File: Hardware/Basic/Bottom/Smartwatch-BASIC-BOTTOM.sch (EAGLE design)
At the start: 35 parts, among them U1 AD5242-SO16, U3 PCF8523

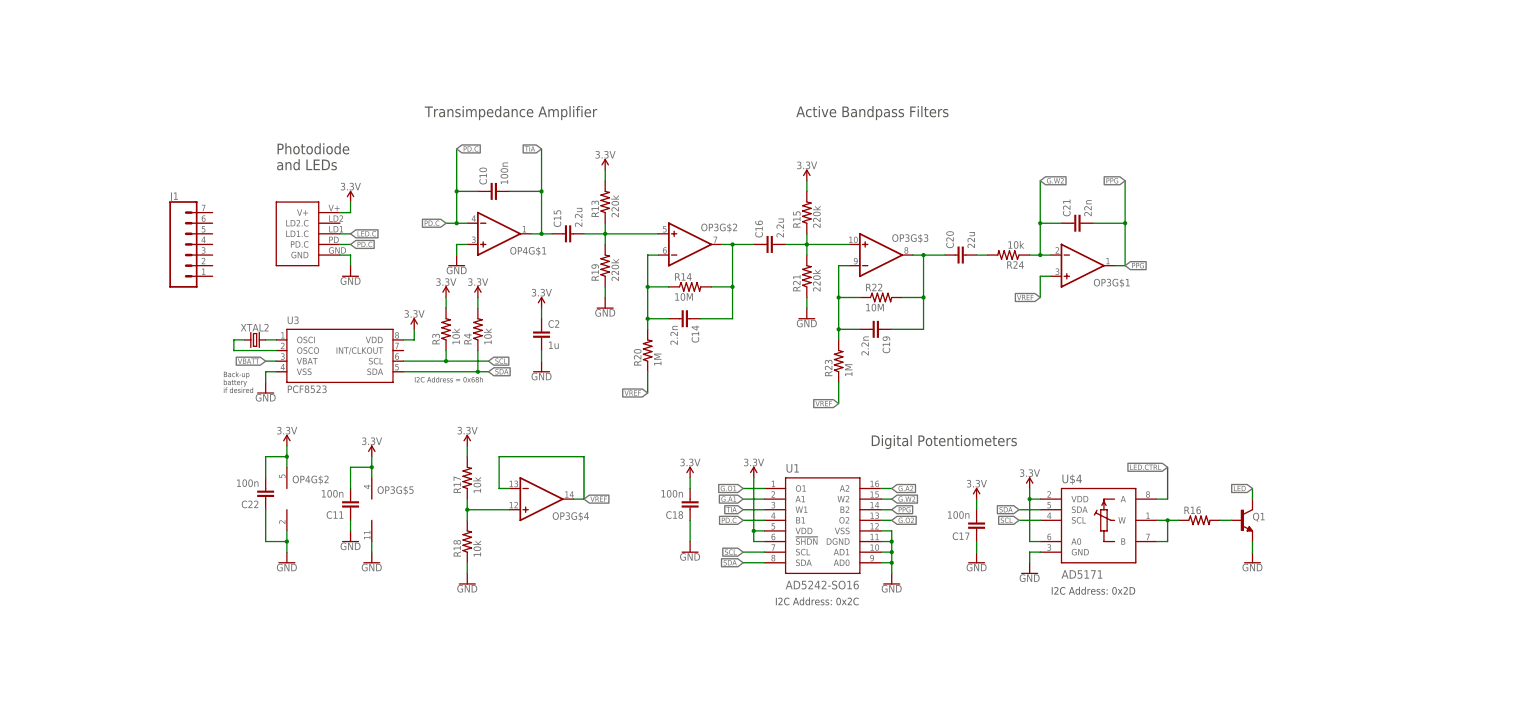
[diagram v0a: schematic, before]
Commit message: Bottom board routed
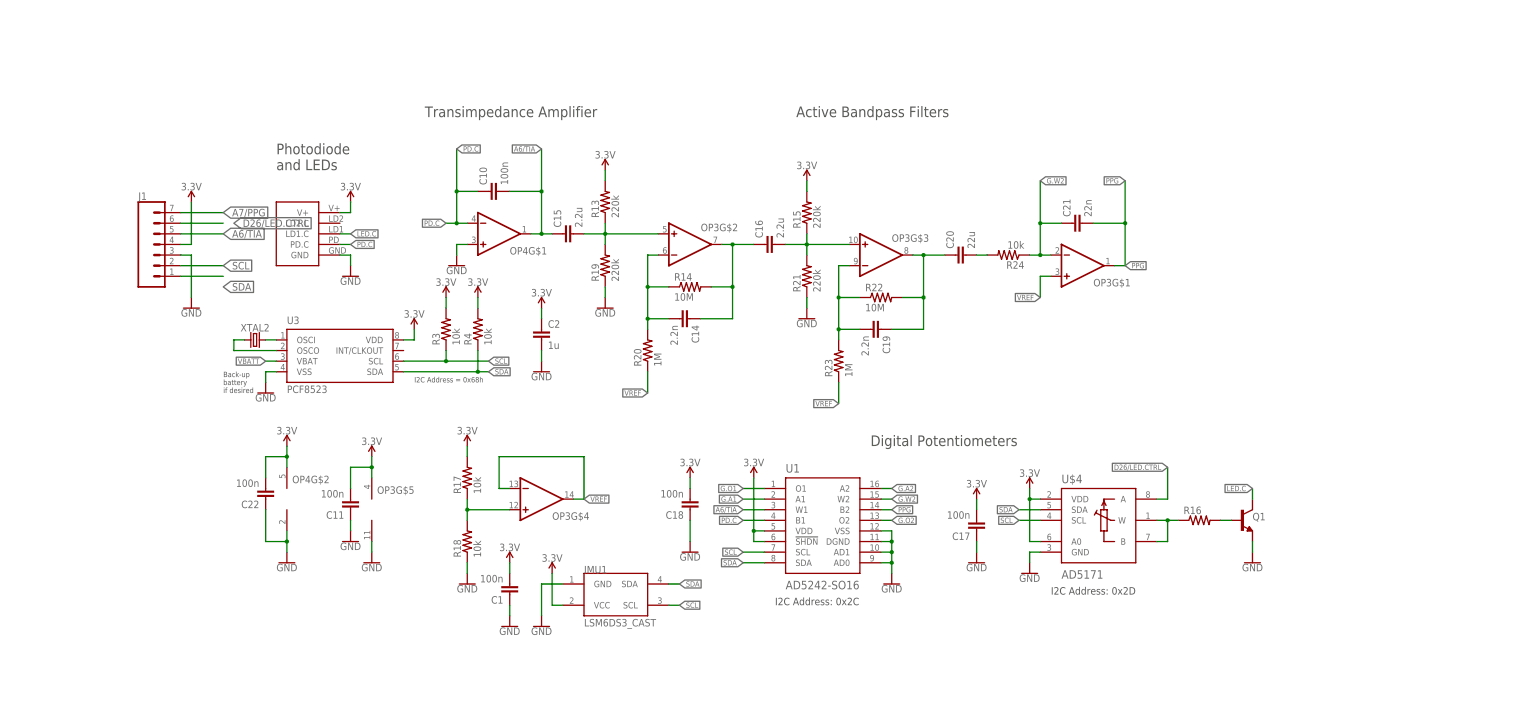
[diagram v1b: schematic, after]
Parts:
- added C1: 100n, LinnesLab-Passives:CAPACITOR0603
- added IMU1: LSM6DS3_CAST, LinnesLab-Sensors:LSM6DS3_CAST
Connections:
- removed net LED: Q1.C
- removed net LED.CTRL: U$4.A
- removed net TIA: C10.2, C15.1, OP4G$1.OUT, U1.W1
- new net A6/TIA: C10.2, C15.1, J1.5, OP4G$1.OUT, U1.W1
- new net A7/PPG: J1.7
- new net D26/LED.CTRL: J1.6, U$4.A
- net 3.3V: now also C1.2, IMU1.VCC, J1.4
- net GND: now also C1.1, IMU1.GND, J1.3
- net LED.C: now also Q1.C
- net SCL: now also IMU1.SCL, J1.2
- net SDA: now also IMU1.SDA, J1.1
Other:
- moved on the sheet: J1

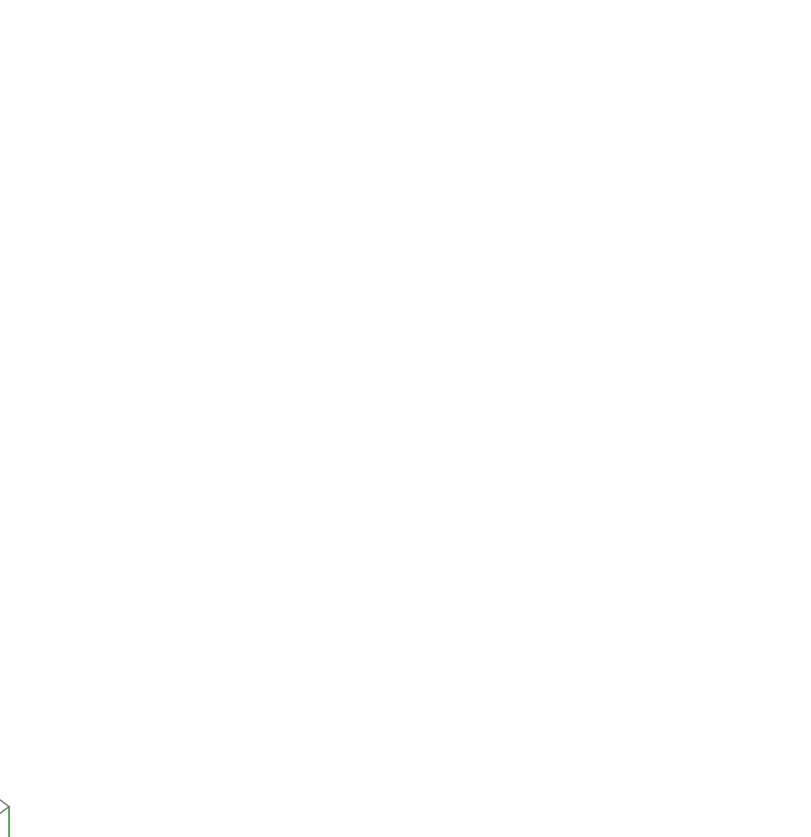
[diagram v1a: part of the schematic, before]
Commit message: Rearranging Top Board
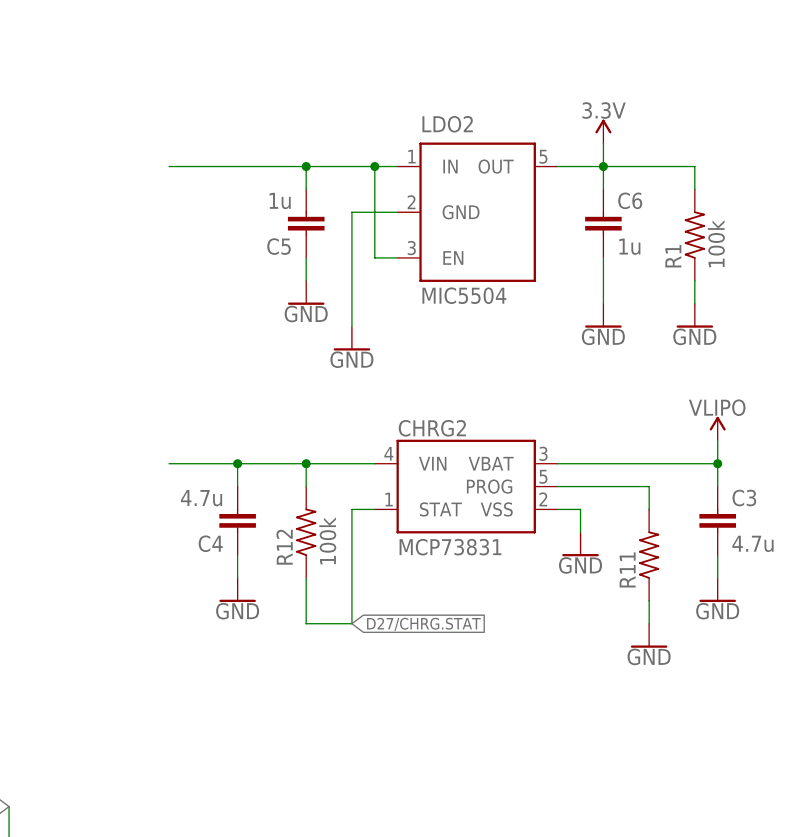
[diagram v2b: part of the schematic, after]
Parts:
- added C3, C4: 4.7u, LinnesLab-Passives:CAPACITOR0603
- added C5, C6: 1u, LinnesLab-Passives:CAPACITOR0603
- added CHRG2: MCP73831, LinnesLab-Power:MCP73831
- added LDO2: MIC5504, LinnesLab-Power:MIC5504
- added R1, R12: 100k, LinnesLab-Passives:RESISTOR0603
- added R11: (no value), LinnesLab-Passives:RESISTOR0603
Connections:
- new net D27/CHRG.STAT: CHRG2.STAT, R12.1
- new net N$1: CHRG2.PROG, R11.2
- new net VIN1: C4.2, C5.2, CHRG2.VIN, LDO2.EN, LDO2.IN, R12.2
- new net VLIPO: C3.1, CHRG2.VBAT
- net 3.3V: now also C6.1, LDO2.OUT, R1.2
- net GND: now also C3.2, C4.1, C5.1, C6.2, CHRG2.VSS, LDO2.GND, R1.1, R11.1

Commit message: Rearranged Top Board
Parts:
- removed C3, C4: 4.7u, LinnesLab-Passives:CAPACITOR0603
- removed C5, C6: 1u, LinnesLab-Passives:CAPACITOR0603
- removed CHRG2: MCP73831, LinnesLab-Power:MCP73831
- removed LDO2: MIC5504, LinnesLab-Power:MIC5504
- removed R1, R12: 100k, LinnesLab-Passives:RESISTOR0603
- removed R11: (no value), LinnesLab-Passives:RESISTOR0603
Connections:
- removed net D27/CHRG.STAT: CHRG2.STAT, R12.1
- removed net N$1: CHRG2.PROG, R11.2
- removed net VIN1: C4.2, C5.2, CHRG2.VIN, LDO2.EN, LDO2.IN, R12.2
- removed net VLIPO: C3.1, CHRG2.VBAT
- net 3.3V: no longer C6.1, LDO2.OUT, R1.2
- net GND: no longer C3.2, C4.1, C5.1, C6.2, CHRG2.VSS, LDO2.GND, R1.1, R11.1

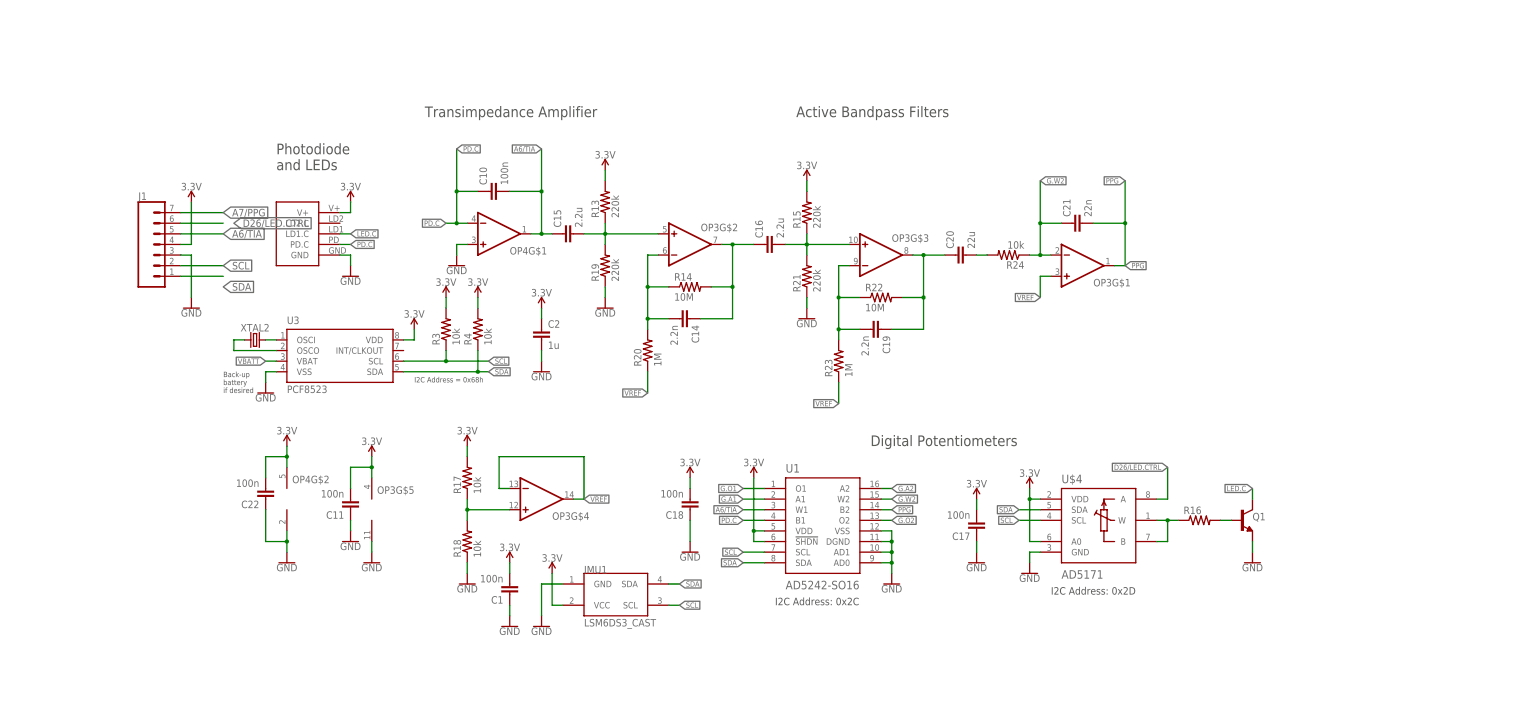
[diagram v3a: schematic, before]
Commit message: Organized Schematics and Silkscreens for both boards
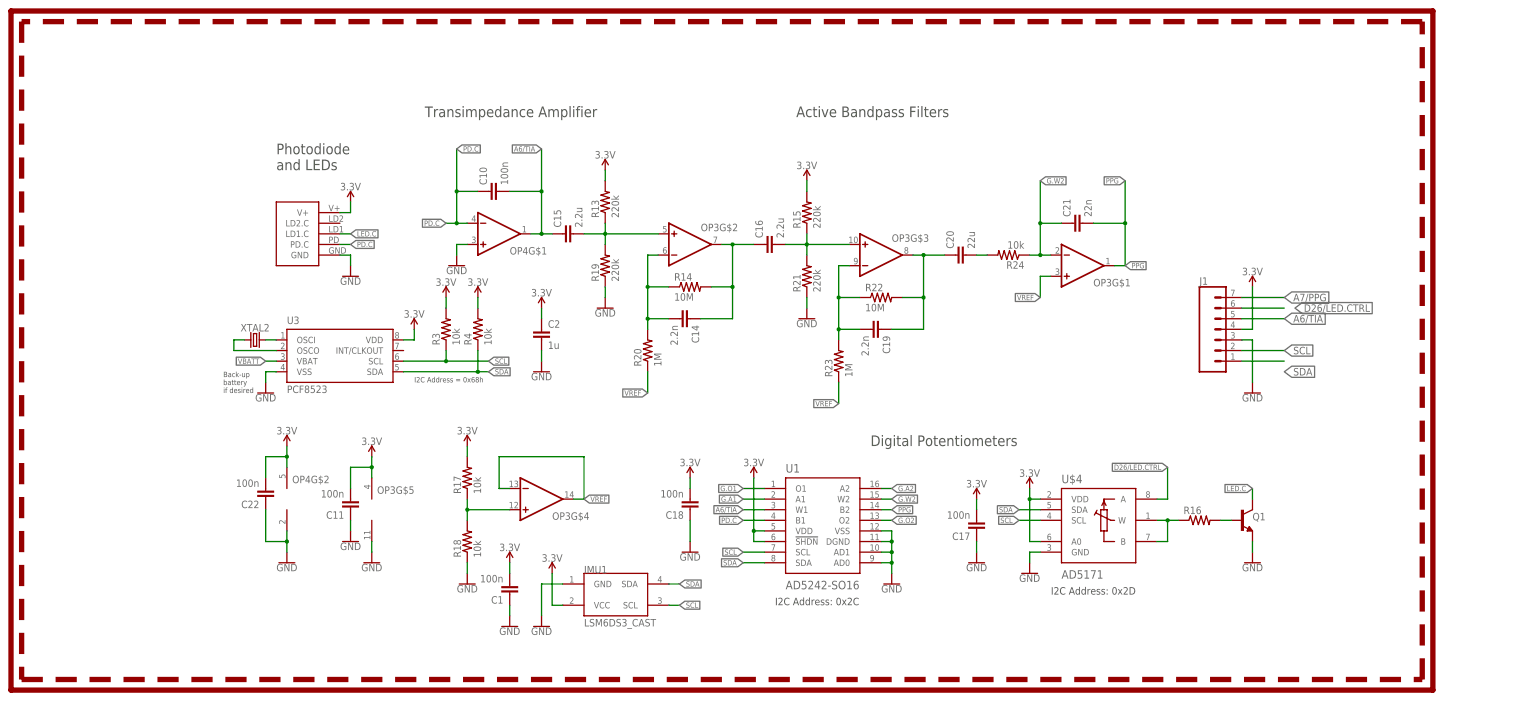
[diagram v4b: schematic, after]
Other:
- moved on the sheet: J1
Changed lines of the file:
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@@
 battery
 if desired</text>
+<wire x1="-114.3" y1="114.3" x2="-114.3" y2="-43.18" width="1.27" layer="94" style="longdash"/>
+<wire x1="-114.3" y1="-43.18" x2="220.98" y2="-43.18" width="1.27" layer="94" style="longdash"/>
+<wire x1="220.98" y1="-43.18" x2="220.98" y2="114.3" width="1.27" layer="94" style="longdash"/>
+<wire x1="220.98" y1="114.3" x2="-114.3" y2="114.3" width="1.27" layer="94" style="longdash"/>
+<wire x1="-116.84" y1="116.84" x2="223.52" y2="116.84" width="1.27" layer="94"/>
+<wire x1="223.52" y1="116.84" x2="223.52" y2="-45.72" width="1.27" layer="94"/>
+<wire x1="223.52" y1="-45.72" x2="-116.84" y2="-45.72" width="1.27" layer="94"/>
+<wire x1="-116.84" y1="-45.72" x2="-116.84" y2="116.84" width="1.27" layer="94"/>
 </plain>
 <instances>
@@
 <attribute name="MFN_MANUFACTURER" x="-38.1" y="35.56" size="1.27" layer="96" display="off"/>
 </instance>
-<instance part="J1" gate="G$1" x="-81.28" y="58.42" smashed="yes">
-<attribute name="VALUE" x="-86.36" y="48.514" size="1.778" layer="96" font="vector"/>
-<attribute name="NAME" x="-86.36" y="71.628" size="1.778" layer="95" font="vector"/>
+<instance part="J1" gate="G$1" x="172.72" y="38.1" smashed="yes">
+<attribute name="VALUE" x="167.64" y="28.194" size="1.778" layer="96" font="vector"/>
+<attribute name="NAME" x="167.64" y="51.308" size="1.778" layer="95" font="vector"/>
 </instance>
 <instance part="IMU1" gate="G$1" x="27.94" y="-22.86" smashed="yes">
@@
 <attribute name="VALUE" x="2.54" y="-12.446" size="1.778" layer="96" align="bottom-center"/>
 </instance>
-<instance part="GND6" gate="G$1" x="-73.66" y="45.72" smashed="yes">
-<attribute name="VALUE" x="-73.66" y="45.466" size="1.778" layer="96" align="top-center"/>
-</instance>
-<instance part="SUPPLY1" gate="G$1" x="-73.66" y="71.12" smashed="yes">
-<attribute name="VALUE" x="-73.66" y="73.914" size="1.778" layer="96" align="bottom-center"/>
+<instance part="GND6" gate="G$1" x="180.34" y="25.4" smashed="yes">
+<attribute name="VALUE" x="180.34" y="25.146" size="1.778" layer="96" align="top-center"/>
+</instance>
+<instance part="SUPPLY1" gate="G$1" x="180.34" y="50.8" smashed="yes">
+<attribute name="VALUE" x="180.34" y="53.594" size="1.778" layer="96" align="bottom-center"/>
 </instance>
 </instances>
@@
 <pinref part="J1" gate="G$1" pin="3"/>
 <pinref part="GND6" gate="G$1" pin="GND"/>
-<wire x1="-76.2" y1="58.42" x2="-73.66" y2="58.42" width="0.1524" layer="91"/>
-<wire x1="-73.66" y1="58.42" x2="-73.66" y2="48.26" width="0.1524" layer="91"/>
+<wire x1="177.8" y1="38.1" x2="180.34" y2="38.1" width="0.1524" layer="91"/>
+<wire x1="180.34" y1="38.1" x2="180.34" y2="27.94" width="0.1524" layer="91"/>
 </segment>
 </net>
@@
 <pinref part="J1" gate="G$1" pin="4"/>
 <pinref part="SUPPLY1" gate="G$1" pin="3.3V"/>
-<wire x1="-76.2" y1="60.96" x2="-73.66" y2="60.96" width="0.1524" layer="91"/>
-<wire x1="-73.66" y1="60.96" x2="-73.66" y2="71.12" width="0.1524" layer="91"/>
+<wire x1="177.8" y1="40.64" x2="180.34" y2="40.64" width="0.1524" layer="91"/>
+<wire x1="180.34" y1="40.64" x2="180.34" y2="50.8" width="0.1524" layer="91"/>
 </segment>
 </net>
@@
 <segment>
 <pinref part="J1" gate="G$1" pin="1"/>
-<wire x1="-76.2" y1="53.34" x2="-66.04" y2="53.34" width="0.1524" layer="91"/>
-<label x="-66.04" y="50.8" size="1.778" layer="95" xref="yes"/>
+<wire x1="177.8" y1="33.02" x2="187.96" y2="33.02" width="0.1524" layer="91"/>
+<label x="187.96" y="30.48" size="1.778" layer="95" xref="yes"/>
 </segment>
 </net>
@@
 <segment>
 <pinref part="J1" gate="G$1" pin="2"/>
-<wire x1="-76.2" y1="55.88" x2="-66.04" y2="55.88" width="0.1524" layer="91"/>
-<label x="-66.04" y="55.88" size="1.778" layer="95" xref="yes"/>
+<wire x1="177.8" y1="35.56" x2="187.96" y2="35.56" width="0.1524" layer="91"/>
+<label x="187.96" y="35.56" size="1.778" layer="95" xref="yes"/>
 </segment>
 </net>
@@
 <segment>
 <pinref part="J1" gate="G$1" pin="5"/>
-<wire x1="-76.2" y1="63.5" x2="-66.04" y2="63.5" width="0.1524" layer="91"/>
-<label x="-66.04" y="63.5" size="1.778" layer="95" xref="yes"/>
+<wire x1="177.8" y1="43.18" x2="187.96" y2="43.18" width="0.1524" layer="91"/>
+<label x="187.96" y="43.18" size="1.778" layer="95" xref="yes"/>
 </segment>
 </net>
@@
 <segment>
 <pinref part="J1" gate="G$1" pin="7"/>
-<wire x1="-76.2" y1="68.58" x2="-66.04" y2="68.58" width="0.1524" layer="91"/>
-<label x="-66.04" y="68.58" size="1.778" layer="95" xref="yes"/>
+<wire x1="177.8" y1="48.26" x2="187.96" y2="48.26" width="0.1524" layer="91"/>
+<label x="187.96" y="48.26" size="1.778" layer="95" xref="yes"/>
 </segment>
 </net>
@@
 <segment>
 <pinref part="J1" gate="G$1" pin="6"/>
-<wire x1="-76.2" y1="66.04" x2="-66.04" y2="66.04" width="0.1524" layer="91"/>
-<label x="-63.5" y="66.04" size="1.778" layer="95" xref="yes"/>
-</segment>
-<segment>
+<wire x1="177.8" y1="45.72" x2="187.96" y2="45.72" width="0.1524" layer="91"/>
+<label x="190.5" y="45.72" size="1.778" layer="95" xref="yes"/>
+</segment>
+<segment>

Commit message: Fixed Top Board Issue
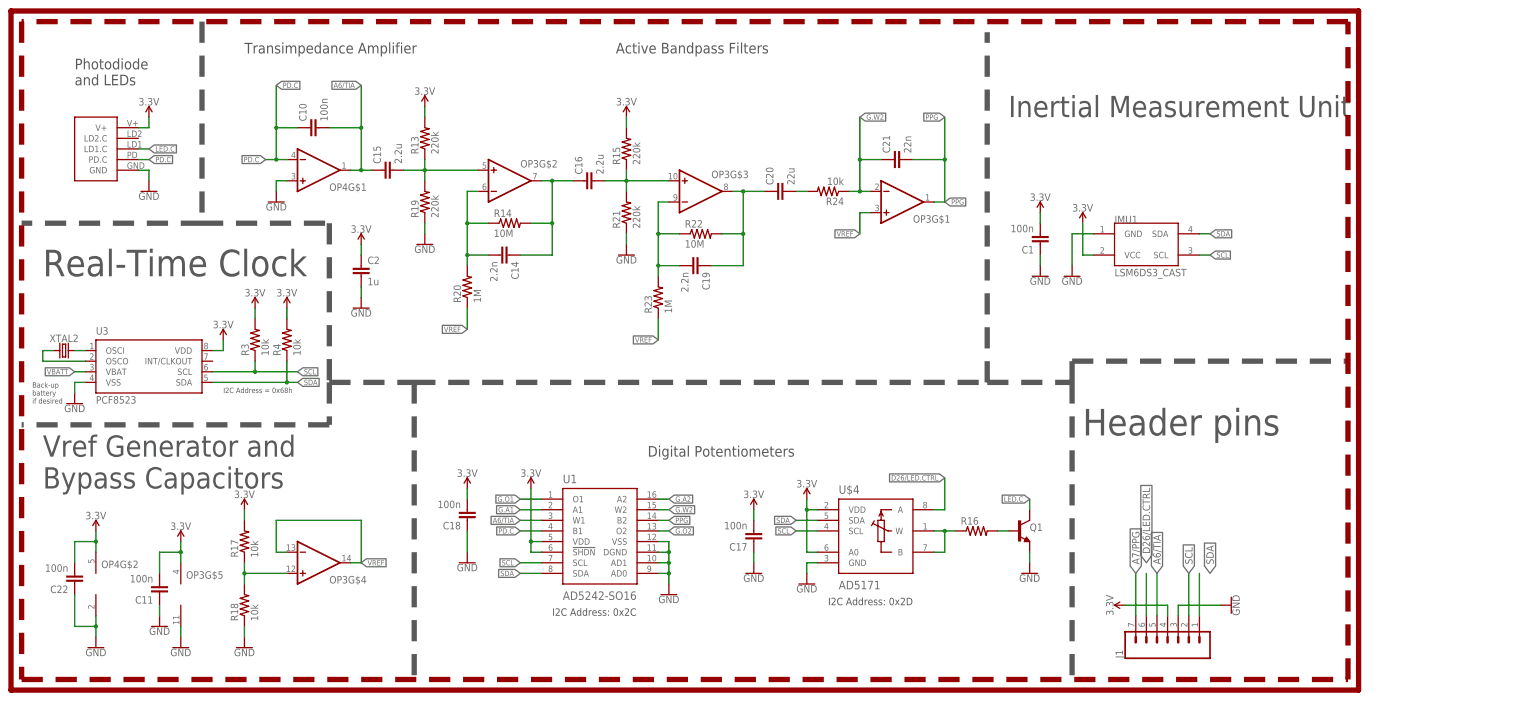
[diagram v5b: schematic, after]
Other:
- note added: "Header pins"
- note added: "Inertial Measurement Unit"
- note added: "Real-Time Clock"
- note added: "Vref Generator and Bypass Capacitors"
- moved on the sheet: C1, C10, C11, C14, C15, C16, C17, C18, C19, C2, C20, C21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

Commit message: Header Pins Fixed
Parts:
- J1: device LinnesLab-Connectors:CONN_07 -> LinnesLab-Connectors:CONN_07-1.27MM
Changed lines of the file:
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@@
 <attribute name="MFN_MANUFACTURER" value="NXP USA Inc."/>
 </part>
-<part name="J1" library="LinnesLab-Connectors" deviceset="CONN_07" device=""/>
+<part name="J1" library="LinnesLab-Connectors" deviceset="CONN_07" device="-1.27MM"/>
 <part name="IMU1" library="LinnesLab-Sensors" deviceset="LSM6DS3_CAST" device=""/>
 <part name="GND1" library="LinnesLab-Symbols" deviceset="GND" device=""/>
